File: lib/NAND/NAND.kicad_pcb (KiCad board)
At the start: 2 copper layers, 4 parts, among them P1 Q_PJFET_GSD, P2 Q_PJFET_GSD

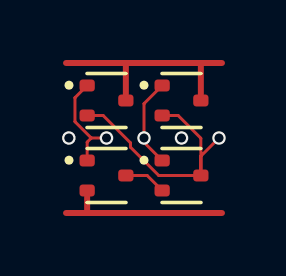
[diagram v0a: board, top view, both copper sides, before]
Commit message: Somehow NAND PCB was botched. Changed pin position of B, too
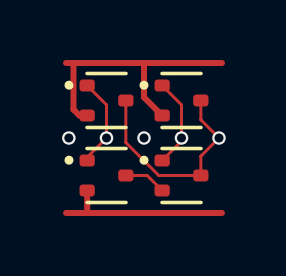
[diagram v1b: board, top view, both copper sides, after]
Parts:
- N1, N2: value Q_NJFET_GSD -> (none)
- P1, P2: value Q_PJFET_GSD -> (none)
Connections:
- net Net-(Q3-D) renamed int1
- P1 pad 2: Y -> VDD
- P1 pad 3: VDD -> Y
- P2 pad 2: Y -> VDD
- P2 pad 3: VDD -> Y
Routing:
- net Y: track 9.16 -> 7.36 mm
- net VDD: track 7.70 -> 9.29 mm
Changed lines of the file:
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@@
 	(net 3 "A")
 	(net 4 "VDD")
-	(net 5 "Net-(Q3-D)")
+	(net 5 "int1")
 	(net 6 "B")
 	(footprint "Package_TO_SOT_SMD:SOT-523"
@@
 			)
 		)
-		(property "Value" "Q_NJFET_GSD"
+		(property "Value" ""
 			(at 0 1.75 0)
 			(layer "F.Fab")
@@
 			(net 6 "B")
 			(pinfunction "G")
-			(pintype "input")
+			(pintype "inout")
 		)
 		(pad "2" smd roundrect
@@
 			(layers "F.Cu" "F.Mask" "F.Paste")
 			(roundrect_rratio 0.25)
-			(net 5 "Net-(Q3-D)")
+			(net 5 "int1")
 			(pinfunction "S")
-			(pintype "passive")
+			(pintype "inout")
 		)
 		(pad "3" smd roundrect
@@
 			(net 1 "Y")
 			(pinfunction "D")
-			(pintype "passive")
+			(pintype "inout")
 		)
 		(embedded_fonts no)
@@
 			)
 		)
-		(property "Value" "Q_PJFET_GSD"
+		(property "Value" ""
 			(at 0 1.75 0)
 			(layer "F.Fab")
@@
 			(net 6 "B")
 			(pinfunction "G")
-			(pintype "input")
+			(pintype "inout")
 		)
 		(pad "2" smd roundrect
@@
 			(layers "F.Cu" "F.Mask" "F.Paste")
 			(roundrect_rratio 0.25)
-			(net 1 "Y")
+			(net 4 "VDD")
 			(pinfunction "S")
-			(pintype "passive")
+			(pintype "inout")
 		)
 		(pad "3" smd roundrect
@@
 			(layers "F.Cu" "F.Mask" "F.Paste")
 			(roundrect_rratio 0.25)
-			(net 4 "VDD")
+			(net 1 "Y")
 			(pinfunction "D")
-			(pintype "passive")
+			(pintype "inout")
 		)
 		(embedded_fonts no)
@@
 			)
 		)
-		(property "Value" "Q_NJFET_GSD"
+		(property "Value" ""
 			(at 0 1.75 0)
 			(layer "F.Fab")
@@
 			(net 3 "A")
 			(pinfunction "G")
-			(pintype "input")
+			(pintype "inout")
 		)
 		(pad "2" smd roundrect
@@
 			(net 2 "GND")
 			(pinfunction "S")
-			(pintype "passive")
+			(pintype "inout")
 		)
 		(pad "3" smd roundrect
@@
 			(layers "F.Cu" "F.Mask" "F.Paste")
 			(roundrect_rratio 0.25)
-			(net 5 "Net-(Q3-D)")
+			(net 5 "int1")
 			(pinfunction "D")
-			(pintype "passive")
+			(pintype "inout")
 		)
 		(embedded_fonts no)
@@
 			)
 		)
-		(property "Value" "Q_PJFET_GSD"
+		(property "Value" ""
 			(at 0 1.75 0)
 			(layer "F.Fab")
@@
 			(net 3 "A")
 			(pinfunction "G")
-			(pintype "input")
+			(pintype "inout")
 		)
 		(pad "2" smd roundrect
@@
 			(layers "F.Cu" "F.Mask" "F.Paste")
 			(roundrect_rratio 0.25)
-			(net 1 "Y")
+			(net 4 "VDD")
 			(pinfunction "S")
-			(pintype "passive")
+			(pintype "inout")
 		)
 		(pad "3" smd roundrect
@@
 			(layers "F.Cu" "F.Mask" "F.Paste")
 			(roundrect_rratio 0.25)
-			(net 4 "VDD")
+			(net 1 "Y")
 			(pinfunction "D")
-			(pintype "passive")
+			(pintype "inout")
 		)
 		(embedded_fonts no)
@@
 			)
 		)
-	)
-	(via
-		(at 3.75 2.5)
-		(size 0.45)
-		(drill 0.3)
-		(layers "F.Cu" "B.Cu")
-		(net 0)
 	)
 	(via
@@
 		(net 0)
 	)
+	(via
+		(at 2.5 2.5)
+		(size 0.45)
+		(drill 0.3)
+		(layers "F.Cu" "B.Cu")
+		(net 0)
+	)
+	(segment
+		(start 1.895 2.652738)
+		(end 1.895 1.25)
+		(width 0.1)
+		(layer "F.Cu")
+		(net 1)
+	)
+	(segment
+		(start 4.395 1.25)
+		(end 4.395 1.895)
+		(width 0.1)
+		(layer "F.Cu")
+		(net 1)
+	)
+	(segment
+		(start 5 2.5)
+		(end 4.395 3.105)
+		(width 0.1)
+		(layer "F.Cu")
+		(net 1)
+	)
 	(segment
 		(start 4.395 3.75)
-		(end 4.395 2.507189)
+		(end 2.992262 3.75)
 		(width 0.1)
 		(layer "F.Cu")
@@
 	)
 	(segment
+		(start 4.395 1.895)
+		(end 5 2.5)
+		(width 0.1)
+		(layer "F.Cu")
+		(net 1)
+	)
+	(segment
+		(start 4.395 3.105)
+		(end 4.395 3.75)
+		(width 0.1)
+		(layer "F.Cu")
+		(net 1)
+	)
+	(segment
 		(start 2.992262 3.75)
-		(end 4.395 3.75)
-		(width 0.1)
-		(layer "F.Cu")
-		(net 1)
-	)
-	(segment
-		(start 4.395 3.75)
-		(end 4.395 3.105)
-		(width 0.1)
-		(layer "F.Cu")
-		(net 1)
-	)
-	(segment
-		(start 2.049 2.806738)
-		(end 2.992262 3.75)
-		(width 0.1)
-		(layer "F.Cu")
-		(net 1)
-	)
-	(segment
-		(start 3.105 1.75)
-		(end 3.105 1.855)
-		(width 0.1)
-		(layer "F.Cu")
-		(net 1)
-	)
-	(segment
-		(start 0.605 1.75)
-		(end 1.137811 1.75)
-		(width 0.1)
-		(layer "F.Cu")
-		(net 1)
-	)
-	(segment
-		(start 2.049 2.661189)
-		(end 2.049 2.806738)
-		(width 0.1)
-		(layer "F.Cu")
-		(net 1)
-	)
-	(segment
-		(start 3.637811 1.75)
-		(end 3.105 1.75)
-		(width 0.1)
-		(layer "F.Cu")
-		(net 1)
-	)
-	(segment
-		(start 1.137811 1.75)
-		(end 2.049 2.661189)
-		(width 0.1)
-		(layer "F.Cu")
-		(net 1)
-	)
-	(segment
-		(start 4.395 2.507189)
-		(end 3.637811 1.75)
-		(width 0.1)
-		(layer "F.Cu")
-		(net 1)
-	)
-	(segment
-		(start 4.395 3.105)
-		(end 5 2.5)
+		(end 1.895 2.652738)
 		(width 0.1)
 		(layer "F.Cu")
@@
 	)
 	(segment
-		(start 0.199 1.156)
-		(end 0.199 1.956738)
+		(start 0.605 0.75)
+		(end 1.25 1.395)
 		(width 0.1)
 		(layer "F.Cu")
@@
 	)
 	(segment
-		(start 0.742262 2.5)
+		(start 1.25 1.395)
 		(end 1.25 2.5)
 		(width 0.1)
@@
 	)
 	(segment
-		(start 0.605 0.75)
-		(end 0.199 1.156)
+		(start 1.25 2.5)
+		(end 0.605 3.145)
 		(width 0.1)
 		(layer "F.Cu")
@@
 	)
 	(segment
-		(start 0.199 1.956738)
-		(end 0.742262 2.5)
-		(width 0.1)
-		(layer "F.Cu")
-		(net 3)
-	)
-	(segment
-		(start 0.742262 2.5)
-		(end 0.605 2.637262)
-		(width 0.1)
-		(layer "F.Cu")
-		(net 3)
-	)
-	(segment
-		(start 0.605 2.637262)
+		(start 0.605 3.145)
 		(end 0.605 3.25)
 		(width 0.1)
@@
 	)
 	(segment
-		(start 4.395 0.005)
-		(end 4.4 0)
+		(start 0.15 1.549999)
+		(end 0.15 0)
 		(width 0.2)
 		(layer "F.Cu")
@@
 	)
 	(segment
-		(start 1.895 1.25)
-		(end 1.895 0.005)
+		(start 0.350001 1.75)
+		(end 0.15 1.549999)
 		(width 0.2)
 		(layer "F.Cu")
@@
 	)
 	(segment
-		(start 4.395 1.25)
-		(end 4.395 0.005)
+		(start 0.605 1.75)
+		(end 0.350001 1.75)
 		(width 0.2)
 		(layer "F.Cu")
@@
 	)
 	(segment
+		(start 3.105 1.75)
+		(end 2.5 1.145)
+		(width 0.2)
+		(layer "F.Cu")
+		(net 4)
+	)
+	(segment
 		(start 1.9 0)
+		(end 2.5 0)
+		(width 0.2)
+		(layer "F.Cu")
+		(net 4)
+	)
+	(segment
+		(start 2.5 1.145)
+		(end 2.5 0)
+		(width 0.2)
+		(layer "F.Cu")
+		(net 4)
+	)
+	(segment
+		(start 2.5 0)
 		(end 4.4 0)
 		(width 0.2)
@@
 	(segment
 		(start -0.1 0)
+		(end 0.15 0)
+		(width 0.2)
+		(layer "F.Cu")
+		(net 4)
+	)
+	(segment
+		(start 0.15 0)
 		(end 1.9 0)
 		(width 0.2)
@@
 	)
 	(segment
-		(start 1.895 0.005)
-		(end 1.9 0)
-		(width 0.2)
-		(layer "F.Cu")
-		(net 4)
+		(start 2.605 3.75)
+		(end 3.105 4.25)
+		(width 0.1)
+		(layer "F.Cu")
+		(net 5)
 	)
 	(segment
@@
 	)
 	(segment
-		(start 2.605 3.75)
-		(end 3.105 4.25)
-		(width 0.1)
-		(layer "F.Cu")
-		(net 5)
-	)
-	(segment
-		(start 2.5 2.5)
-		(end 2.5 2.645)
+		(start 3.75 2.605)
+		(end 3.105 3.25)
 		(width 0.1)
 		(layer "F.Cu")
@@
 	(segment
 		(start 3.105 0.75)
-		(end 2.5 1.355)
+		(end 3.75 1.395)
 		(width 0.1)
 		(layer "F.Cu")
@@
 	)
 	(segment
-		(start 2.5 1.355)
-		(end 2.5 2.5)
+		(start 3.75 1.395)
+		(end 3.75 2.5)
 		(width 0.1)
 		(layer "F.Cu")
@@
 	)
 	(segment
-		(start 2.5 2.645)
-		(end 3.105 3.25)
+		(start 3.75 2.5)
+		(end 3.75 2.605)
 		(width 0.1)
 		(layer "F.Cu")
@@
 	)
 	(via
-		(at 2.5 2.5)
+		(at 3.75 2.5)
 		(size 0.45)
 		(drill 0.3)

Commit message: High-density layout with pitch of 1.1mm, which gains 23% !!
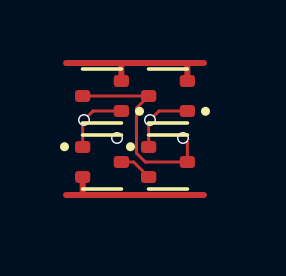
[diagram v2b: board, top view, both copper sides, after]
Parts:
- moved N2 0.64 mm to (3.30, 3.30)
- moved N1 0.47 mm to (1.10, 3.30)
- moved P2 0.47 mm to (3.30, 1.10), turned to 180 degrees
- moved P1 0.21 mm to (1.10, 1.10), turned to 180 degrees
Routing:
- net VDD: track 9.29 -> 5.78 mm
- net GND: track 5.95 -> 5.20 mm
- net A: track 3.03 -> 2.29 mm
- net B: track 3.03 -> 2.29 mm
- net (no net): vias 2 -> 1
